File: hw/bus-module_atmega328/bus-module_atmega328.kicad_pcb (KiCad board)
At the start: 2 copper layers, 35 x 48 mm, 32 parts, among them J1 CONN_10X2, J2 CONN_7X2, J3 CONN-ISP-6, J5 CONN_1, J6 CONN_1, J7 CONN_1, J8 CONN_1, U1 ATMEGA328-TQFP32, U2 7,3728MHz, U3 25LC256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

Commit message: R2, R3, R4 100 Ohms
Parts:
- R2, R3, R4: value 1k -> 100
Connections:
- D2 pad 2: (no net) -> Net-(D2-Pad2)
- H1 pad 1: (no net) -> Net-(H1-Pad1)
- J1 pad 11: (no net) -> Net-(J1-Pad11)
- J1 pad 17: (no net) -> Net-(J1-Pad17)
- J1 pad 19: (no net) -> Net-(J1-Pad19)
- J1 pad 20: (no net) -> Net-(J1-Pad20)
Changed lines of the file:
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@@
-(kicad_pcb (version 20171130) (host pcbnew 5.0.0-fee4fd1~66~ubuntu16.04.1)
+(kicad_pcb (version 20171130) (host pcbnew 5.0.2-bee76a0~70~ubuntu18.04.1)
   (general
     (thickness 1.6)
@@
     (zones 0)
     (modules 32)
-    (nets 39)
+    (nets 45)
   )
   (page A4)
@@
     (pad_drill 2.5)
     (pad_to_mask_clearance 0)
+    (solder_mask_min_width 0.25)
     (aux_axis_origin 0 0)
     (grid_origin 88.575 83.41)
@@
   (net 37 /B)
   (net 38 "Net-(F1-Pad1)")
+  (net 39 "Net-(D2-Pad2)")
+  (net 40 "Net-(H1-Pad1)")
+  (net 41 "Net-(J1-Pad11)")
+  (net 42 "Net-(J1-Pad17)")
+  (net 43 "Net-(J1-Pad19)")
+  (net 44 "Net-(J1-Pad20)")
   (net_class Default "This is the default net class."
     (clearance 0.2)
@@
     (add_net "Net-(C1-Pad1)")
     (add_net "Net-(C2-Pad1)")
+    (add_net "Net-(D2-Pad2)")
     (add_net "Net-(F1-Pad1)")
+    (add_net "Net-(H1-Pad1)")
+    (add_net "Net-(J1-Pad11)")
+    (add_net "Net-(J1-Pad17)")
+    (add_net "Net-(J1-Pad19)")
+    (add_net "Net-(J1-Pad20)")
     (add_net "Net-(R1-Pad2)")
     (add_net "Net-(R5-Pad2)")
@@
     (add_net +24V)
     (add_net GND)
-    (add_net "Net-(F1-Pad2)")
   )
   (module Inductor:L_0805 (layer F.Cu)
@@
       (effects (font (size 0.8 0.8) (thickness 0.15)))
     )
-    (fp_text value 1k (at 0.127 1.524 270) (layer F.Fab)
+    (fp_text value 100 (at 0.127 1.524 270) (layer F.Fab)
       (effects (font (size 0.8 0.8) (thickness 0.15)))
     )
@@
       (effects (font (size 0.8 0.8) (thickness 0.15)))
     )
-    (fp_text value 1k (at 0.127 1.524 270) (layer F.Fab)
+    (fp_text value 100 (at 0.127 1.524 270) (layer F.Fab)
       (effects (font (size 0.8 0.8) (thickness 0.15)))
     )
@@
       (effects (font (size 0.8 0.8) (thickness 0.15)))
     )
-    (fp_text value 1k (at 0.127 1.524 270) (layer F.Fab)
+    (fp_text value 100 (at 0.127 1.524 270) (layer F.Fab)
       (effects (font (size 0.8 0.8) (thickness 0.15)))
     )
@@
     (pad 10 thru_hole circle (at -1.27 -1.27) (size 1.6002 1.6002) (drill 1.016) (layers *.Cu *.Mask F.SilkS)
       (net 14 /PC4))
-    (pad 11 thru_hole circle (at 1.27 1.27) (size 1.6002 1.6002) (drill 1.016) (layers *.Cu *.Mask F.SilkS))
+    (pad 11 thru_hole circle (at 1.27 1.27) (size 1.6002 1.6002) (drill 1.016) (layers *.Cu *.Mask F.SilkS)
+      (net 41 "Net-(J1-Pad11)"))
     (pad 12 thru_hole circle (at 1.27 -1.27) (size 1.6002 1.6002) (drill 1.016) (layers *.Cu *.Mask F.SilkS)
       (net 25 //RESET))
@@
     (pad 16 thru_hole circle (at 6.35 -1.27) (size 1.524 1.524) (drill 1.016) (layers *.Cu *.Mask F.SilkS)
       (net 17 /PD5))
-    (pad 17 thru_hole circle (at 8.89 1.27) (size 1.524 1.524) (drill 1.016) (layers *.Cu *.Mask F.SilkS))
+    (pad 17 thru_hole circle (at 8.89 1.27) (size 1.524 1.524) (drill 1.016) (layers *.Cu *.Mask F.SilkS)
+      (net 42 "Net-(J1-Pad17)"))
     (pad 18 thru_hole circle (at 8.89 -1.27) (size 1.524 1.524) (drill 1.016) (layers *.Cu *.Mask F.SilkS)
       (net 18 /PD7))
-    (pad 19 thru_hole circle (at 11.43 1.27) (size 1.524 1.524) (drill 1.016) (layers *.Cu *.Mask F.SilkS))
-    (pad 20 thru_hole circle (at 11.43 -1.27) (size 1.524 1.524) (drill 1.016) (layers *.Cu *.Mask F.SilkS))
+    (pad 19 thru_hole circle (at 11.43 1.27) (size 1.524 1.524) (drill 1.016) (layers *.Cu *.Mask F.SilkS)
+      (net 43 "Net-(J1-Pad19)"))
+    (pad 20 thru_hole circle (at 11.43 -1.27) (size 1.524 1.524) (drill 1.016) (layers *.Cu *.Mask F.SilkS)
+      (net 44 "Net-(J1-Pad20)"))
   )
   (module Capacitors_SMD:C_0805 (layer F.Cu)
@@
     (pad 3 smd rect (at 0.95 -0.95 90) (size 0.85 0.85) (layers F.Cu F.Paste F.Mask)
       (net 37 /B))
-    (pad 2 smd rect (at 0.95 0.95 90) (size 0.85 0.85) (layers F.Cu F.Paste F.Mask))
+    (pad 2 smd rect (at 0.95 0.95 90) (size 0.85 0.85) (layers F.Cu F.Paste F.Mask)
+      (net 39 "Net-(D2-Pad2)"))
     (pad 1 smd rect (at -0.76962 0.95 90) (size 1.2 0.85) (layers F.Cu F.Paste F.Mask)
       (net 1 GND))
@@
     (fp_line (start -2.54 2.54) (end 2.54 2.54) (layer F.SilkS) (width 0.254))
     (fp_line (start 2.54 2.54) (end 2.54 -2.54) (layer F.SilkS) (width 0.254))
-    (pad 1 thru_hole circle (at 0 0) (size 3.5 3.5) (drill 2.5) (layers *.Cu *.Mask F.SilkS))
+    (pad 1 thru_hole circle (at 0 0) (size 3.5 3.5) (drill 2.5) (layers *.Cu *.Mask F.SilkS)
+      (net 40 "Net-(H1-Pad1)"))
   )
   (module Symbol:Symbol_OSHW-Logo_SilkScreen (layer B.Cu)

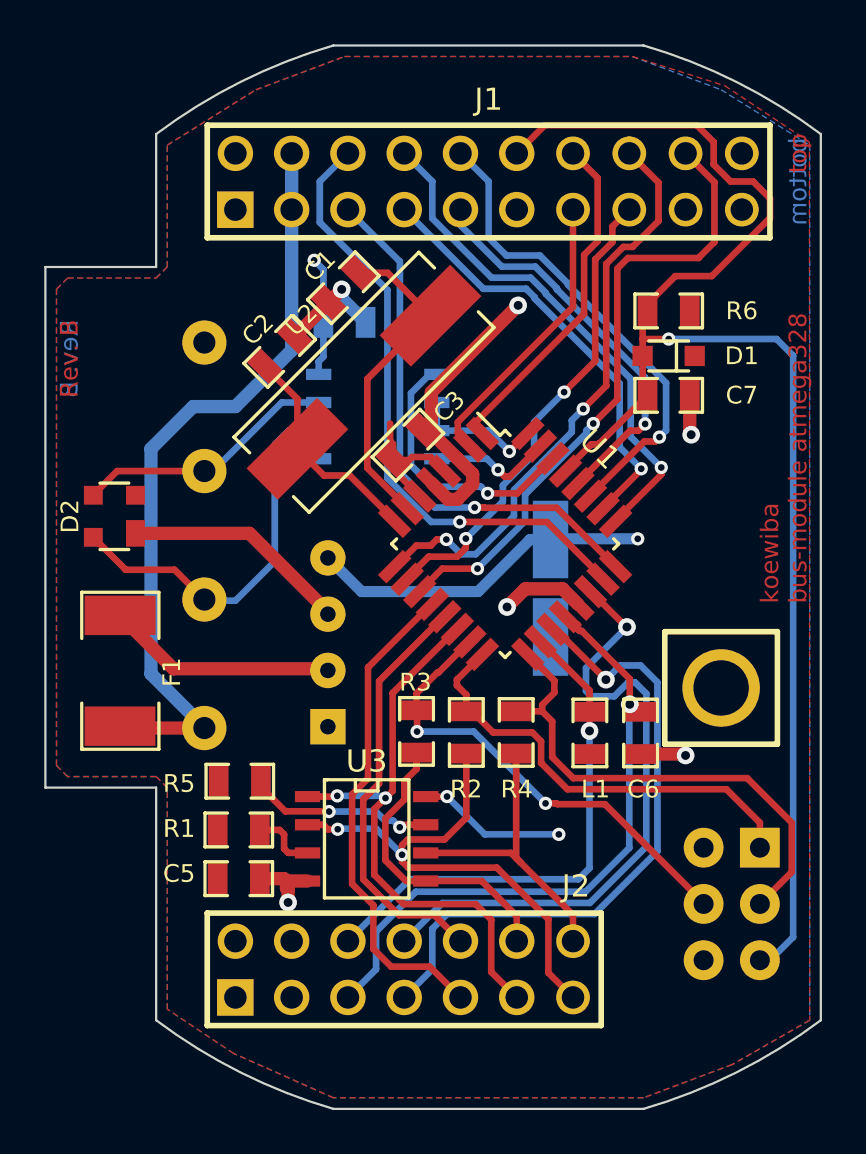
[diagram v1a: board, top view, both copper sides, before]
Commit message: Increase WAGO hole diameter, replace ELKO with keramic capacitor, Increase WAGO hole diameter, update footprints, update footprints, set Rev to C
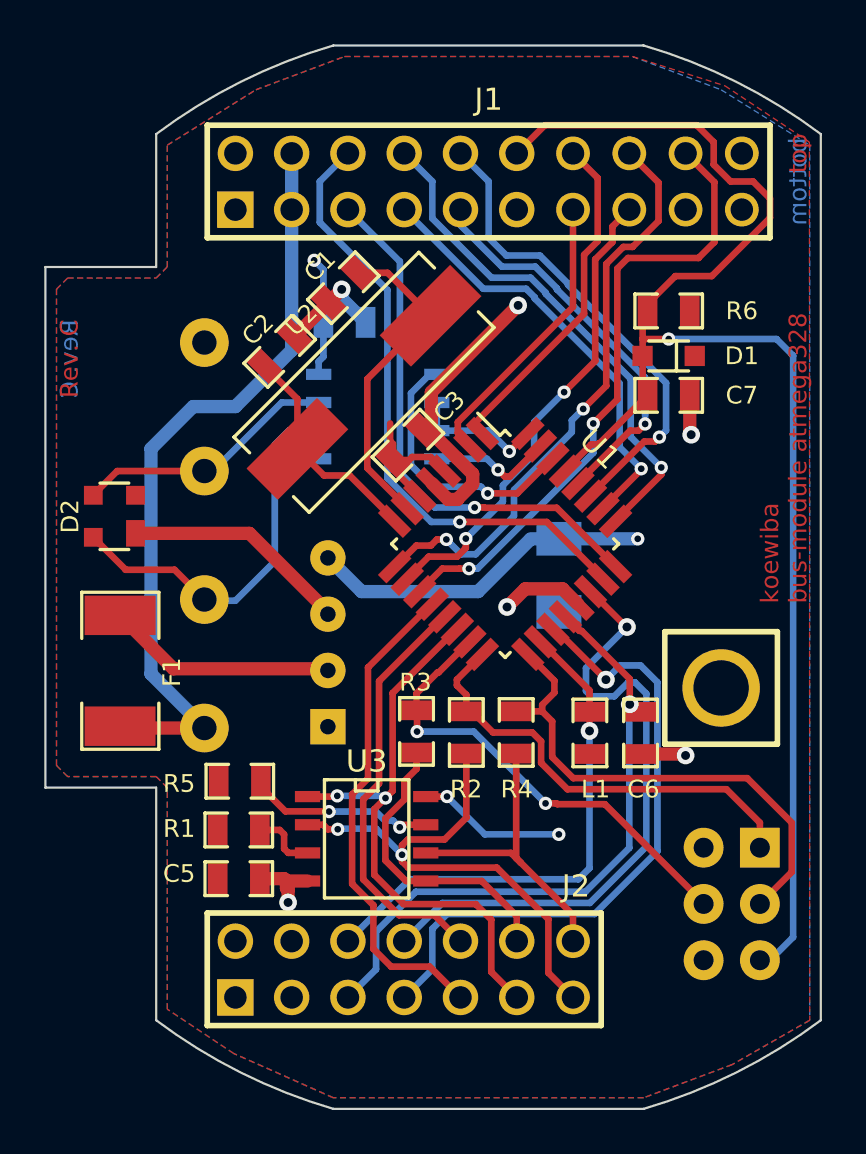
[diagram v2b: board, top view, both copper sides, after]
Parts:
- C9: value 100µF -> 100µF/6,3V VS; footprint Capacitors_SMD:CP_D6.3mm -> Capacitors_SMD:C_1206
- moved C9 0.69 mm to (103.2, 99.9), turned to 270 degrees
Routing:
- net VCC: track 34.4 -> 35.3 mm
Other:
- rule trace_min: 0.2 -> 0.3
- board text added: "Rev. C"
- board text removed: "Rev. B"

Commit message: Update to KiCAD6: bus-module_atmega328
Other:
- net class Default removed
- net class Power removed
